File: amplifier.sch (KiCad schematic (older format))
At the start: 1 part

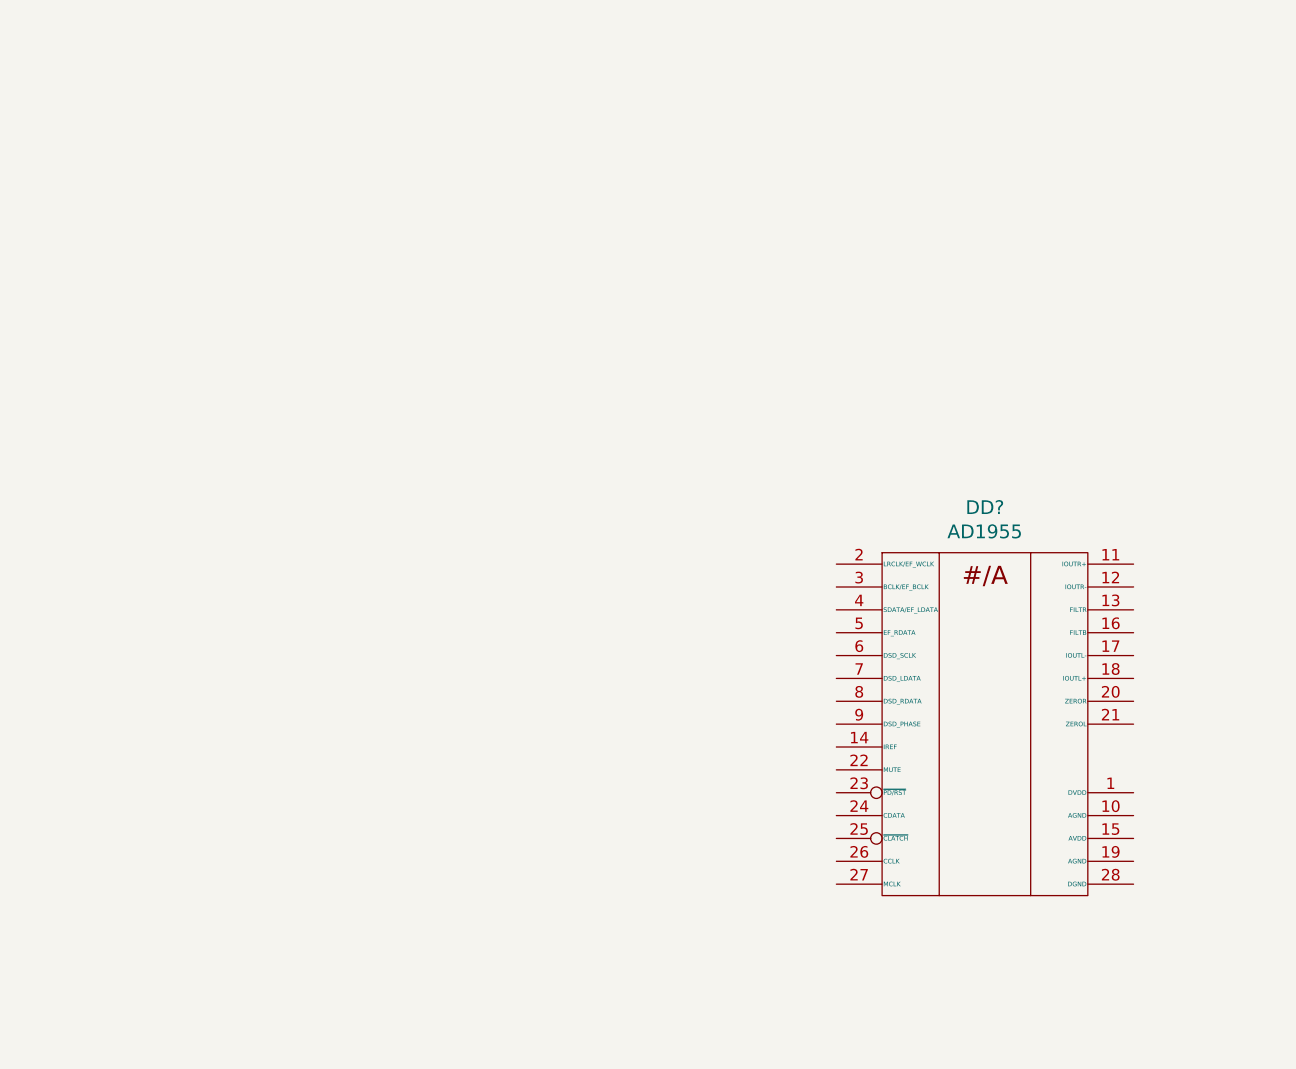
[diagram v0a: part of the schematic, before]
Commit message: Add src4392i model
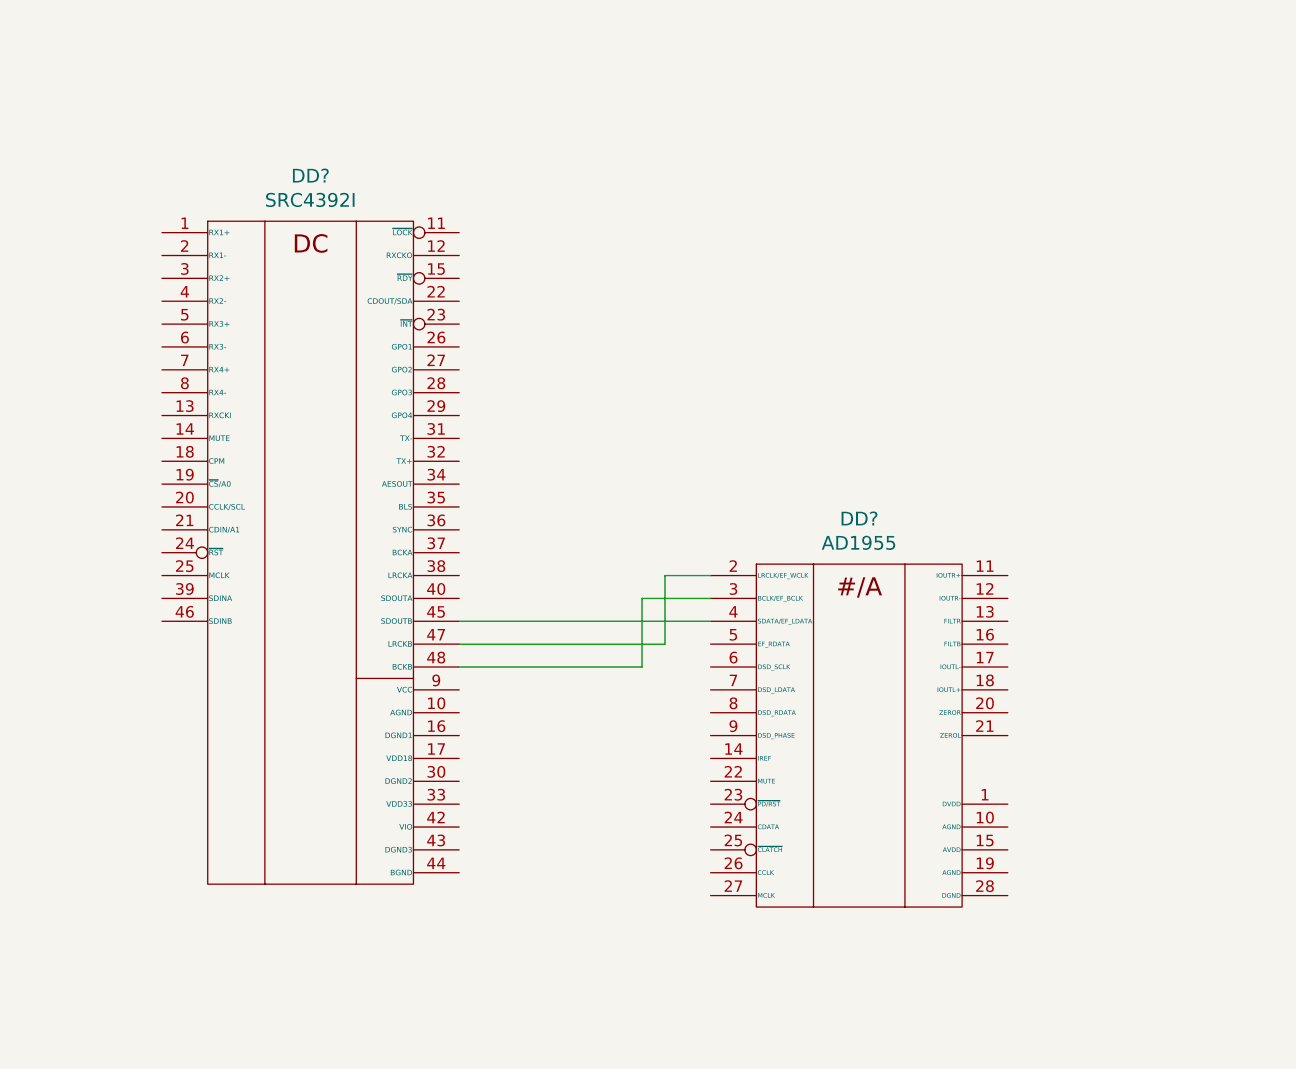
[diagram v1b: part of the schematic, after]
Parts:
- removed DD?: AD1955, symbol AD1955
- added DD?: AD1955, symbol AD1955
- added DD?: SRC4392I, symbol SRC4392I
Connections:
- new net: DD?.2 (LRCLK/EF_WCLK), DD?.47 (LRCKB)
- new net: DD?.3 (BCLK/EF_BCLK), DD?.48 (BCKB)
- new net: DD?.4 (SDATA/EF_LDATA), DD?.45 (SDOUTB)
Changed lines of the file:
@@
 LIBS:tda7293v
 LIBS:ad1955
+LIBS:src4392i
 LIBS:amplifier-cache
 EELAYER 26 0
@@
 $Descr A4 11693 8268
 encoding utf-8
-Sheet 1 3
+Sheet 1 4
 Title ""
 Date ""
@@
 $Comp
 L AD1955 DD?
-U 1 1 5942591C
-P 6700 3350
-F 0 "DD?" H 6700 4297 60  0000 C CNN
-F 1 "AD1955" H 6700 4191 60  0000 C CNN
-F 2 "" H 6700 3600 60  0001 C CNN
-F 3 "" H 6700 3600 60  0001 C CNN
-	1    6700 3350
+U 1 1 5943ADF1
+P 6150 3400
+F 0 "DD?" H 6150 4347 60  0000 C CNN
+F 1 "AD1955" H 6150 4241 60  0000 C CNN
+F 2 "" H 6150 3650 60  0001 C CNN
+F 3 "" H 6150 3650 60  0001 C CNN
+	1    6150 3400
 	1    0    0    -1
 $EndComp
+$Comp
+L SRC4392I DD?
+U 1 1 5943BE8C
+P 3750 2650
+F 0 "DD?" H 3750 4347 60  0000 C CNN
+F 1 "SRC4392I" H 3750 4241 60  0000 C CNN
+F 2 "" H 3800 3350 60  0001 C CNN
+F 3 "" H 3800 3350 60  0001 C CNN
+	1    3750 2650
+	1    0    0    -1
+$EndComp
+Wire Wire Line
+	5500 2900 4400 2900
+Wire Wire Line
+	4400 3000 5300 3000
+Wire Wire Line
+	5300 3000 5300 2700
+Wire Wire Line
+	5300 2700 5500 2700
+Wire Wire Line
+	5500 2800 5200 2800
+Wire Wire Line
+	5200 2800 5200 3100
+Wire Wire Line
+	5200 3100 4400 3100
 $EndSCHEMATC

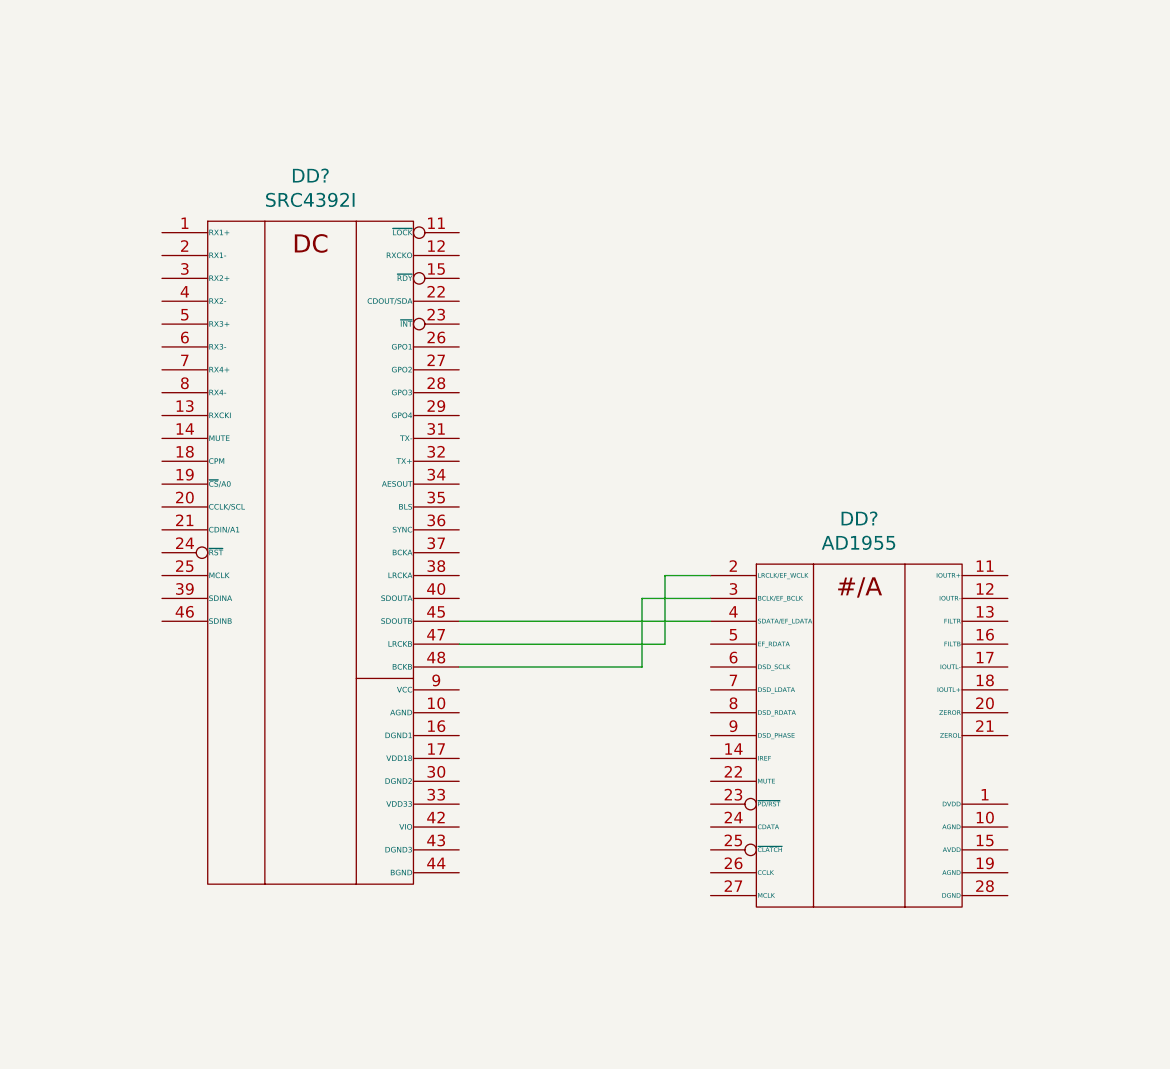
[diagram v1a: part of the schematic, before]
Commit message: Move DAC circuit from amplifier.sch to DAC.sch
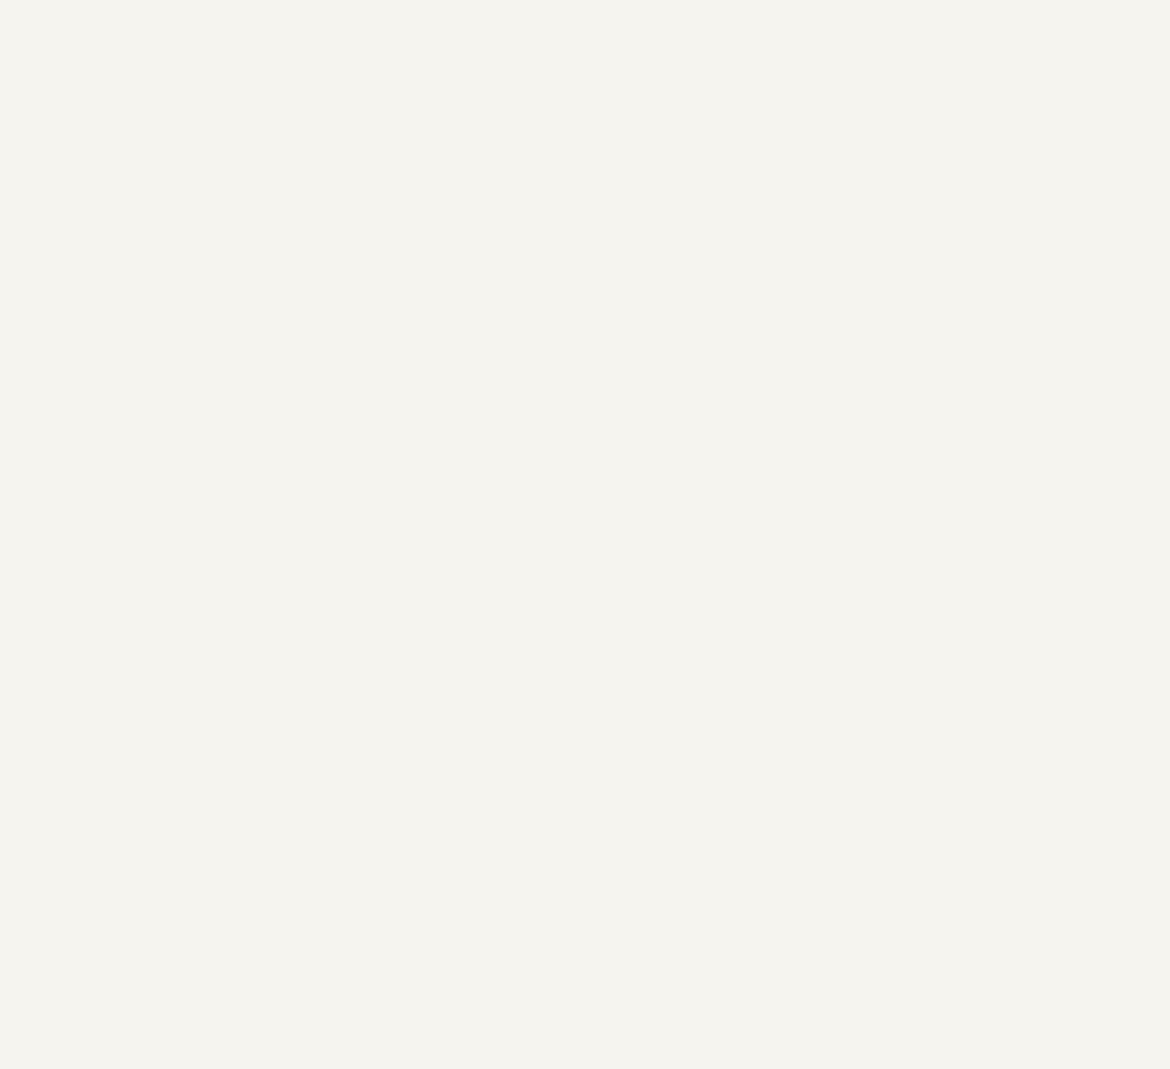
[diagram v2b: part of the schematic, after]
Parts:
- removed DD?: AD1955, symbol AD1955
- removed DD?: SRC4392I, symbol SRC4392I
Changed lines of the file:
@@
 F1 "PowerAmplifier.sch" 60
 $EndSheet
-$Comp
-L AD1955 DD?
-U 1 1 5943ADF1
-P 6150 3400
-F 0 "DD?" H 6150 4347 60  0000 C CNN
-F 1 "AD1955" H 6150 4241 60  0000 C CNN
-F 2 "" H 6150 3650 60  0001 C CNN
-F 3 "" H 6150 3650 60  0001 C CNN
-	1    6150 3400
-	1    0    0    -1
-$EndComp
-$Comp
-L SRC4392I DD?
-U 1 1 5943BE8C
-P 3750 2650
-F 0 "DD?" H 3750 4347 60  0000 C CNN
-F 1 "SRC4392I" H 3750 4241 60  0000 C CNN
-F 2 "" H 3800 3350 60  0001 C CNN
-F 3 "" H 3800 3350 60  0001 C CNN
-	1    3750 2650
-	1    0    0    -1
-$EndComp
-Wire Wire Line
-	5500 2900 4400 2900
-Wire Wire Line
-	4400 3000 5300 3000
-Wire Wire Line
-	5300 3000 5300 2700
-Wire Wire Line
-	5300 2700 5500 2700
-Wire Wire Line
-	5500 2800 5200 2800
-Wire Wire Line
-	5200 2800 5200 3100
-Wire Wire Line
-	5200 3100 4400 3100
 $EndSCHEMATC

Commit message: Update DAC
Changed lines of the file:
@@
-EESchema Schematic File Version 2
-LIBS:amplifier-rescue
-LIBS:ad1955
-LIBS:cdclvc1104
-LIBS:kc7050
-LIBS:lp5900
-LIBS:src4392i
-LIBS:tda7293v
-LIBS:74xgxx
-LIBS:74xx
-LIBS:ac-dc
-LIBS:adc-dac
-LIBS:analog_switches
-LIBS:atmel
-LIBS:audio
-LIBS:brooktre
-LIBS:cmos4000
-LIBS:cmos_ieee
-LIBS:conn
-LIBS:contrib
-LIBS:cypress
-LIBS:dc-dc
-LIBS:device
-LIBS:digital-audio
-LIBS:display
-LIBS:dsp
-LIBS:elec-unifil
-LIBS:ftdi
-LIBS:gennum
-LIBS:graphic
-LIBS:hc11
-LIBS:intel
-LIBS:interface
-LIBS:linear
-LIBS:logo
-LIBS:memory
-LIBS:microchip
-LIBS:microchip1
-LIBS:microchip_pic10mcu
-LIBS:microchip_pic12mcu
-LIBS:microchip_pic16mcu
-LIBS:microcontrollers
-LIBS:motorola
-LIBS:msp430
-LIBS:nxp_armmcu
-LIBS:opto
-LIBS:philips
-LIBS:power
-LIBS:powerint
-LIBS:pspice
-LIBS:references
-LIBS:regul
-LIBS:relays
-LIBS:sensors
-LIBS:siliconi
-LIBS:special
-LIBS:stm8
-LIBS:stm32
-LIBS:supertex
-LIBS:texas
-LIBS:transf
-LIBS:transistors
-LIBS:ttl_ieee
-LIBS:valves
-LIBS:video
-LIBS:xilinx
-LIBS:ad8066
-LIBS:ldk220
-LIBS:+9va
+EESchema Schematic File Version 4
 LIBS:amplifier-cache
-EELAYER 25 0
+EELAYER 26 0
 EELAYER END
 $Descr A4 11693 8268
 encoding utf-8
-Sheet 1 4
+Sheet 1 5
 Title ""
 Date ""
@@
 F1 "PowerAmplifier.sch" 60
 $EndSheet
+$Sheet
+S 0    -300 11650 8800
+U 5C997C50
+F0 "Spectrum Analyzer" 50
+F1 "spectrum_analyzer.sch" 50
+$EndSheet
 $EndSCHEMATC
